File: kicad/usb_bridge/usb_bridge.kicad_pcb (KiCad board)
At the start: 4 copper layers, 40 x 40 mm, 34 parts, among them J1 Conn_01x02_Male, J2 UJ2-BH-1-TH, J3 Conn_01x04_Male, J4 Conn_01x01_Male, J5 Conn_01x07_Male, U1 SRV05-4, U2 AMS1117-3.3, U3 STM32F730R8, X1 QX7

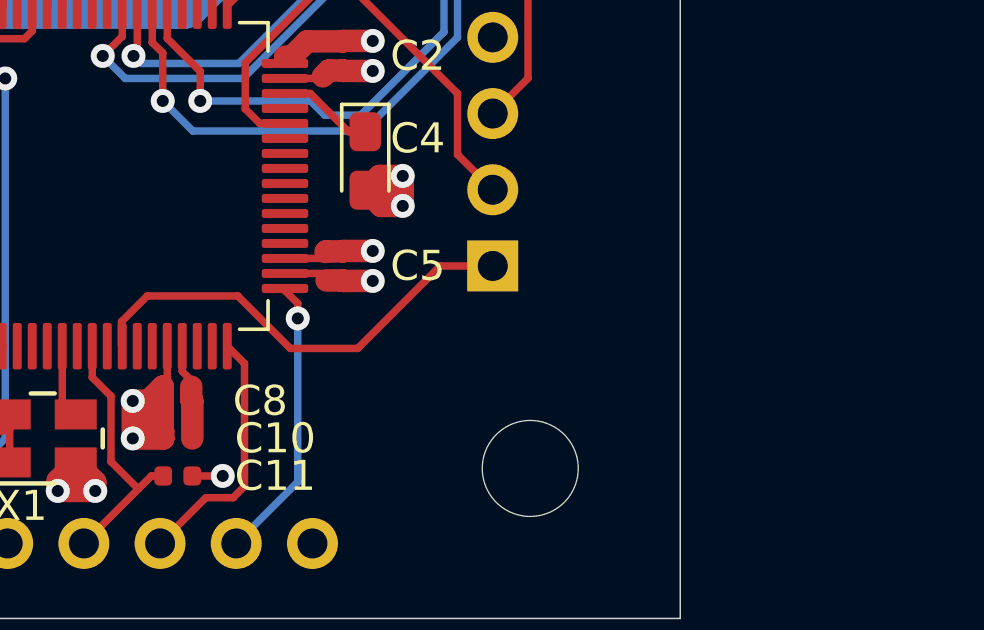
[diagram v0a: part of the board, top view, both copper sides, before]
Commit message: Schematic bugfixes
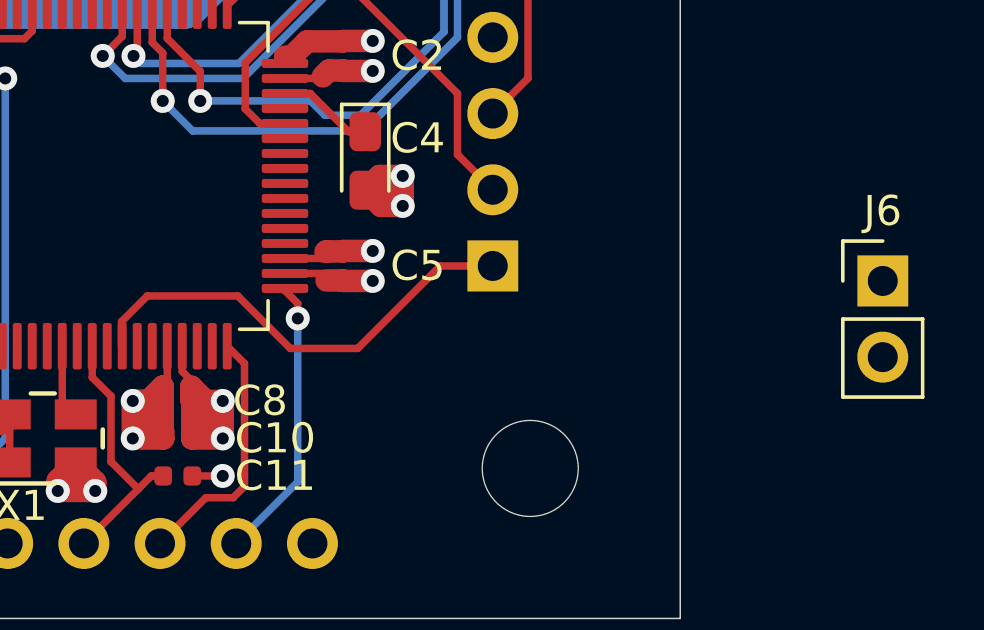
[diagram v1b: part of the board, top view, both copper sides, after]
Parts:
- added J6: Conn_01x02_Male, Connector_PinHeader_2.54mm:PinHeader_1x02_P2.54mm_Vertical, F.Cu at (176.8, 98.8)
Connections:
- C10 pad 1: Net-(C10-Pad1) -> +3V3
- C8 pad 1: Net-(C10-Pad1) -> +3V3
- U3 pad 13: Net-(C10-Pad1) -> +3V3
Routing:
- net +3V3: track 22.1 -> 30.9 mm, vias 15 -> 17
- net Net-(C10-Pad1): track 3.70 -> 0.00 mm
